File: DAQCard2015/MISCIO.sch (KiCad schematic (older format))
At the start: 25 parts, among them K1 1462042-8, P3 miniDIL20, P4 LEMO_EPY.00.250.NTN, P5 LEMO_EPY.00.250.NTN, P6 FAN, P9 SMA, Q1 Q_NPN_BCE, Q2 NPN, U24 MCP65R41

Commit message: Various updates to DAQ board focusing on power system
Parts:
- removed D3: LED, symbol LED
- removed JP1: JUMPER, symbol JUMPER
- removed P9: SMA, symbol BNC
- added D1: Dialight_5690101372F, extras:Dialight_5690101372F, symbol Dialight_5690101372F
- added P9: SHV, extras:TE_1217133-1, symbol SHV
- added R50, R51, R52: R, Resistors_SMD:R_0603, symbol R
- C70: footprint (none) -> Capacitors_SMD:C_1812
- D2: footprint (none) -> Diodes_SMD:SMA_Standard
- K1: footprint (none) -> extras:1462042-8
- Q2: footprint (none) -> Housings_SOT-23_SOT-143_TSOT-6:SOT-23
- R55: footprint Resistors_SMD:R_0805 -> Resistors_SMD:R_1206
- R57, R58, R59, R60: footprint (none) -> Resistors_SMD:R_1206
- R61, R62: footprint (none) -> Resistors_SMD:R_0603
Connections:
- net labels added: LED0, LED1
- wire segments 81 -> 84
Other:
- note added: "HV Rated > 600V"
- note removed: "HV Rated > 250V"
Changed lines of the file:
@@
 $EndComp
 $Comp
-L GND #PWR1
+L GND #PWR01
 U 1 1 55F022ED
 P 8100 5400
-F 0 "#PWR1" H 8100 5150 50  0001 C CNN
+F 0 "#PWR01" H 8100 5150 50  0001 C CNN
 F 1 "GND" H 8100 5250 50  0000 C CNN
 F 2 "" H 8100 5400 60  0000 C CNN
@@
 $EndComp
 $Comp
-L GND #PWR2
+L GND #PWR02
 U 1 1 55F02317
 P 8600 5300
-F 0 "#PWR2" H 8600 5050 50  0001 C CNN
+F 0 "#PWR02" H 8600 5050 50  0001 C CNN
 F 1 "GND" H 8600 5150 50  0000 C CNN
 F 2 "" H 8600 5300 60  0000 C CNN
@@
 F 0 "R55" V 9130 4950 50  0000 C CNN
 F 1 "50k" V 9050 4950 50  0000 C CNN
-F 2 "Resistors_SMD:R_0805" V 8980 4950 30  0001 C CNN
+F 2 "Resistors_SMD:R_1206" V 8980 4950 30  0001 C CNN
 F 3 "" H 9050 4950 30  0000 C CNN
 	1    9050 4950
@@
 F 0 "K1" H 3400 2500 60  0000 C CNN
 F 1 "1462042-8" H 3200 1900 60  0000 C CNN
-F 2 "" H 3200 2200 60  0001 C CNN
+F 2 "extras:1462042-8" H 3200 2200 60  0001 C CNN
 F 3 "" H 3200 2200 60  0000 C CNN
 	1    3200 2200
@@
 F 0 "R59" V 2630 2050 50  0000 C CNN
 F 1 "470k" V 2550 2050 50  0000 C CNN
-F 2 "" V 2480 2050 30  0001 C CNN
+F 2 "Resistors_SMD:R_1206" V 2480 2050 30  0001 C CNN
 F 3 "" H 2550 2050 30  0000 C CNN
 	1    2550 2050
@@
 F 0 "R57" V 2330 2400 50  0000 C CNN
 F 1 "470k" V 2250 2400 50  0000 C CNN
-F 2 "" V 2180 2400 30  0001 C CNN
+F 2 "Resistors_SMD:R_1206" V 2180 2400 30  0001 C CNN
 F 3 "" H 2250 2400 30  0000 C CNN
 	1    2250 2400
 	0    1    1    0
 $EndComp
-$Comp
-L BNC P9
-U 1 1 55F41081
-P 1800 2150
-F 0 "P9" H 1810 2270 50  0000 C CNN
-F 1 "SMA" V 1910 2090 50  0000 C CNN
-F 2 "" H 1800 2150 60  0001 C CNN
-F 3 "" H 1800 2150 60  0000 C CNN
-	1    1800 2150
-	-1   0    0    -1
-$EndComp
-Text GLabel 2750 2600 1    60   Input ~ 0
+Text GLabel 1350 2400 0    60   Input ~ 0
 GND
 $Comp
@@
 F 0 "C70" H 1625 2700 50  0000 L CNN
 F 1 "22nF" H 1625 2500 50  0000 L CNN
-F 2 "" H 1638 2450 30  0001 C CNN
+F 2 "Capacitors_SMD:C_1812" H 1638 2450 30  0001 C CNN
 F 3 "" H 1600 2600 60  0000 C CNN
 	1    1600 2600
@@
 F 0 "R60" V 2780 2800 50  0000 C CNN
 F 1 "51k" V 2700 2800 50  0000 C CNN
-F 2 "" V 2630 2800 30  0001 C CNN
+F 2 "Resistors_SMD:R_1206" V 2630 2800 30  0001 C CNN
 F 3 "" H 2700 2800 30  0000 C CNN
 	1    2700 2800
@@
 F 0 "R58" V 2380 2800 50  0000 C CNN
 F 1 "51k" V 2300 2800 50  0000 C CNN
-F 2 "" V 2230 2800 30  0001 C CNN
+F 2 "Resistors_SMD:R_1206" V 2230 2800 30  0001 C CNN
 F 3 "" H 2300 2800 30  0000 C CNN
 	1    2300 2800
@@
 F 0 "D2" H 3900 2580 50  0000 L CNN
 F 1 "D" H 3950 2400 50  0000 L CNN
-F 2 "" V 3950 2500 60  0001 C CNN
+F 2 "Diodes_SMD:SMA_Standard" V 3950 2500 60  0001 C CNN
 F 3 "" V 3950 2500 60  0000 C CNN
 	1    3950 2500
@@
 F 0 "Q2" H 4350 3000 50  0000 R CNN
 F 1 "NPN" H 4400 2900 50  0000 R CNN
-F 2 "" H 4250 3050 29  0001 C CNN
+F 2 "Housings_SOT-23_SOT-143_TSOT-6:SOT-23" H 4250 3050 29  0001 C CNN
 F 3 "" H 4050 2950 60  0000 C CNN
 	1    4050 2950
@@
 Text GLabel 3950 3250 3    60   Input ~ 0
 GND
-$Comp
-L LED D3
-U 1 1 55F438E7
-P 5150 3200
-F 0 "D3" H 5150 3300 50  0000 C CNN
-F 1 "LED" H 5150 3100 50  0000 C CNN
-F 2 "" H 5150 3200 60  0001 C CNN
-F 3 "" H 5150 3200 60  0000 C CNN
-	1    5150 3200
-	0    -1   -1   0
-$EndComp
-$Comp
-L R R62
-U 1 1 55F43A0B
-P 4850 2950
-F 0 "R62" V 4930 2950 50  0000 C CNN
-F 1 "R" V 4850 2950 50  0000 C CNN
-F 2 "" V 4780 2950 30  0001 C CNN
-F 3 "" H 4850 2950 30  0000 C CNN
-	1    4850 2950
-	0    1    1    0
-$EndComp
-Text GLabel 5150 3450 3    60   Input ~ 0
-GND
-Text Label 4600 2650 0    60   ~ 0
-HV_control
 Text GLabel 3950 2100 1    60   Input ~ 0
 5Vdig
@@
 	2400 2050 2400 2400
 Wire Wire Line
-	1600 2400 2100 2400
+	1350 2400 2100 2400
 Wire Wire Line
 	3500 2100 3700 2100
@@
 	1600 2800 1600 2750
 Connection ~ 1600 2800
-Connection ~ 1800 2400
-Wire Wire Line
-	1800 2350 1800 2600
 Wire Wire Line
 	1950 2150 2900 2150
-Wire Wire Line
-	1800 2600 2150 2600
 Wire Wire Line
 	2900 2350 2900 2650
@@
 Wire Wire Line
 	3950 3150 3950 3250
-Wire Wire Line
-	5150 2950 5150 3000
-Wire Wire Line
-	5150 2950 5000 2950
-Wire Wire Line
-	4700 2950 4600 2950
-Wire Wire Line
-	5150 3400 5150 3450
-Wire Wire Line
-	4600 2950 4600 2650
-Connection ~ 4600 2950
-$Comp
-L JUMPER JP1
-U 1 1 55F41215
-P 2450 2600
-F 0 "JP1" H 2450 2750 50  0000 C CNN
-F 1 "JUMPER" H 2450 2520 50  0000 C CNN
-F 2 "" H 2450 2600 60  0001 C CNN
-F 3 "" H 2450 2600 60  0000 C CNN
-	1    2450 2600
-	1    0    0    -1
-$EndComp
 Text Notes 650  2650 0    60   ~ 0
-HV Rated > 250V
+HV Rated > 600V
 $Comp
 L R R61
@@
 F 0 "R61" V 4530 2950 50  0000 C CNN
 F 1 "5k1" V 4450 2950 50  0000 C CNN
-F 2 "" V 4380 2950 30  0001 C CNN
+F 2 "Resistors_SMD:R_0603" V 4380 2950 30  0001 C CNN
 F 3 "" H 4450 2950 30  0000 C CNN
 	1    4450 2950
@@
 Wire Wire Line
 	4300 2950 4250 2950
+$Comp
+L SHV P9
+U 1 1 55F913FA
+P 1800 2150
+F 0 "P9" H 1810 2270 50  0000 C CNN
+F 1 "SHV" H 1900 2050 50  0000 C CNN
+F 2 "extras:TE_1217133-1" H 1800 2150 60  0001 C CNN
+F 3 "" H 1800 2150 60  0000 C CNN
+	1    1800 2150
+	-1   0    0    1
+$EndComp
+Connection ~ 1600 2400
+$Comp
+L Dialight_5690101372F D1
+U 1 1 55FA5BD1
+P 1750 5050
+F 0 "D1" V 1650 5050 60  0000 C CNN
+F 1 "Dialight_5690101372F" V 1900 5050 60  0001 C CNN
+F 2 "extras:Dialight_5690101372F" H 1750 5050 60  0001 C CNN
+F 3 "" H 1750 5050 60  0000 C CNN
+	1    1750 5050
+	1    0    0    -1
+$EndComp
+$Comp
+L Dialight_5690101372F D1
+U 3 1 55FA5D9B
+P 2350 5050
+F 0 "D1" V 2250 5050 60  0000 C CNN
+F 1 "Dialight_5690101372F" V 2500 5050 60  0001 C CNN
+F 2 "extras:Dialight_5690101372F" H 2350 5050 60  0001 C CNN
+F 3 "" H 2350 5050 60  0000 C CNN
+	3    2350 5050
+	1    0    0    -1
+$EndComp
+$Comp
+L Dialight_5690101372F D1
+U 4 1 55FA5E02
+P 2650 5050
+F 0 "D1" V 2550 5050 60  0000 C CNN
+F 1 "Dialight_5690101372F" V 2800 5050 60  0001 C CNN
+F 2 "extras:Dialight_5690101372F" H 2650 5050 60  0001 C CNN
+F 3 "" H 2650 5050 60  0000 C CNN
+	4    2650 5050
+	1    0    0    -1
+$EndComp
+Text GLabel 1750 4400 1    60   Input ~ 0
+5Vdig
+Wire Wire Line
+	2650 5350 2650 5150
+Wire Wire Line
+	1450 5350 2650 5350
+Text GLabel 1450 5350 0    60   Input ~ 0
+GND
+Wire Wire Line
+	2350 5150 2350 5350
+Connection ~ 2350 5350
+Wire Wire Line
+	2050 5150 2050 5350
+Connection ~ 2050 5350
+Wire Wire Line
+	1750 5150 1750 5350
+Connection ~ 1750 5350
+Text GLabel 4750 2950 2    60   Input ~ 0
+HV_control
+Wire Wire Line
+	4750 2950 4600 2950
+Text GLabel 2050 4400 1    60   Input ~ 0
+HV_control
+$Comp
+L R R50
+U 1 1 55FA73A0
+P 1750 4550
+F 0 "R50" V 1830 4550 50  0000 C CNN
+F 1 "R" V 1750 4550 50  0000 C CNN
+F 2 "Resistors_SMD:R_0603" V 1680 4550 30  0001 C CNN
+F 3 "" H 1750 4550 30  0000 C CNN
+	1    1750 4550
+	1    0    0    -1
+$EndComp
+$Comp
+L R R51
+U 1 1 55FA7424
+P 2050 4550
+F 0 "R51" V 2130 4550 50  0000 C CNN
+F 1 "R" V 2050 4550 50  0000 C CNN
+F 2 "Resistors_SMD:R_0603" V 1980 4550 30  0001 C CNN
+F 3 "" H 2050 4550 30  0000 C CNN
+	1    2050 4550
+	1    0    0    -1
+$EndComp
+$Comp
+L R R52
+U 1 1 55FA749A
+P 2350 4550
+F 0 "R52" V 2430 4550 50  0000 C CNN
+F 1 "R" V 2350 4550 50  0000 C CNN
+F 2 "Resistors_SMD:R_0603" V 2280 4550 30  0001 C CNN
+F 3 "" H 2350 4550 30  0000 C CNN
+	1    2350 4550
+	1    0    0    -1
+$EndComp
+$Comp
+L R R62
+U 1 1 55FA7511
+P 2650 4550
+F 0 "R62" V 2730 4550 50  0000 C CNN
+F 1 "R" V 2650 4550 50  0000 C CNN
+F 2 "Resistors_SMD:R_0603" V 2580 4550 30  0001 C CNN
+F 3 "" H 2650 4550 30  0000 C CNN
+	1    2650 4550
+	1    0    0    -1
+$EndComp
+$Comp
+L Dialight_5690101372F D1
+U 2 1 55FA5C66
+P 2050 5050
+F 0 "D1" V 1950 5050 60  0000 C CNN
+F 1 "Dialight_5690101372F" V 2200 5050 60  0001 C CNN
+F 2 "extras:Dialight_5690101372F" H 2050 5050 60  0001 C CNN
+F 3 "" H 2050 5050 60  0000 C CNN
+	2    2050 5050
+	1    0    0    -1
+$EndComp
+Wire Wire Line
+	1750 4700 1750 4850
+Wire Wire Line
+	2050 4700 2050 4850
+Wire Wire Line
+	2350 4700 2350 4850
+Wire Wire Line
+	2650 4700 2650 4850
+Text GLabel 2350 4400 1    60   Input ~ 0
+LED0
+Text GLabel 2650 4400 1    60   Input ~ 0
+LED1
 $EndSCHEMATC

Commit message: Updates to DAQ board focusing on Support electronics
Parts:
- removed Q1: Q_NPN_BCE, Housings_SOT-23_SOT-143_TSOT-6:SOT-23, symbol Q_NPN_BCE
- added Q1: Q_NPN_BCE_REV, symbol Q_NPN_BCE_REV
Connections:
- wire segments 84 -> 82
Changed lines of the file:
@@
 $Descr A4 11693 8268
 encoding utf-8
-Sheet 12 13
+Sheet 3 13
 Title ""
 Date ""
@@
 $EndComp
 $Comp
-L Q_NPN_BCE Q1
-U 1 1 55F036FA
-P 10200 4650
-F 0 "Q1" H 10500 4700 50  0000 R CNN
-F 1 "Q_NPN_BCE" H 10800 4600 50  0000 R CNN
-F 2 "Housings_SOT-23_SOT-143_TSOT-6:SOT-23" H 10400 4750 29  0001 C CNN
-F 3 "" H 10200 4650 60  0000 C CNN
-	1    10200 4650
-	1    0    0    -1
-$EndComp
-$Comp
 L R R56
 U 1 1 55F03778
@@
 Text GLabel 3950 2100 1    60   Input ~ 0
 5Vdig
-Text Label 1350 2800 0    60   ~ 0
-Vbias
 Wire Wire Line
 	8450 2450 8450 3400
@@
 	8450 2850 8500 2850
 Wire Wire Line
-	10050 1900 9750 1900
-Wire Wire Line
-	9750 1900 9750 2050
-Wire Wire Line
-	9750 2050 9200 2050
-Wire Wire Line
-	9200 2150 9800 2150
-Wire Wire Line
-	9800 2150 9800 2050
-Wire Wire Line
-	9800 2050 10050 2050
+	9200 2050 10050 2050
+Wire Wire Line
+	9800 2150 9200 2150
+Wire Wire Line
+	9800 1900 9800 2150
 Wire Wire Line
 	9200 2250 9750 2250
 Wire Wire Line
-	9750 2250 9750 2500
-Wire Wire Line
-	9750 2500 9800 2500
-Wire Wire Line
-	9800 2650 9700 2650
-Wire Wire Line
-	9700 2650 9700 2350
+	9750 2250 9750 2650
 Wire Wire Line
 	9700 2350 9200 2350
@@
 Text GLabel 2650 4400 1    60   Input ~ 0
 LED1
+$Comp
+L Q_NPN_BCE_REV Q1
+U 1 1 56022DB8
+P 10200 4650
+F 0 "Q1" H 10500 4700 50  0000 R CNN
+F 1 "Q_NPN_BCE_REV" H 11000 4600 50  0000 R CNN
+F 2 "" H 10400 4750 29  0000 C CNN
+F 3 "" H 10200 4650 60  0000 C CNN
+	1    10200 4650
+	1    0    0    -1
+$EndComp
+Text GLabel 1350 2800 0    60   Input ~ 0
+Vbias
+Wire Wire Line
+	9800 1900 10050 1900
+Wire Wire Line
+	9750 2650 9800 2650
+Wire Wire Line
+	9700 2350 9700 2500
+Wire Wire Line
+	9700 2500 9800 2500
 $EndSCHEMATC

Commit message: Adds APC128 connections and voltage supplies
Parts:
- removed Q2: NPN, Housings_SOT-23_SOT-143_TSOT-6:SOT-23, symbol Q_NPN_BCE
- added Q2: SBC817-40LT1G, Housings_SOT-23_SOT-143_TSOT-6:SOT-23, symbol Q_NPN_BCE_REV
- added U19, U23: AD8534, Housings_SSOP:TSSOP-14_4.4x5mm_Pitch0.65mm, symbol AD8534
- added U22: AD5628, extras:TSSOP-16_4.4x5mm_Pitch0.65mm, symbol AD5628
- D2: value D -> SMAJ75A
- Q1: value Q_NPN_BCE_REV -> MMBT2222A-TP; footprint (none) -> Housings_SOT-23_SOT-143_TSOT-6:SOT-23
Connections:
- net labels added: Aref_A, Aref_B, DAC_A, DAC_B, DAC_C, DAC_D, DAC_E, DAC_F, DAC_G, DAC_H, RG_A, RG_B, SPI_SCL, SPI_SDA, SUPDAC_CSB, Vana_A, Vana_B, Vocm, Vthresh
- wire segments 82 -> 123
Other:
- moved on the sheet: C70, D1A, D1B, D1C, D1D, D2, K1, P3, P4, P5, P6, P9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

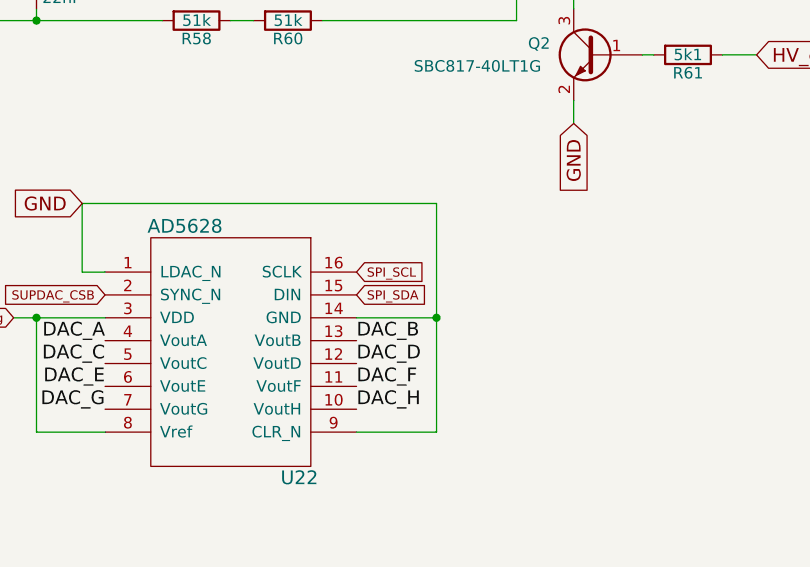
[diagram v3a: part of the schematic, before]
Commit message: Adds misc traces(gnds, SPI, etc) to DAQ board
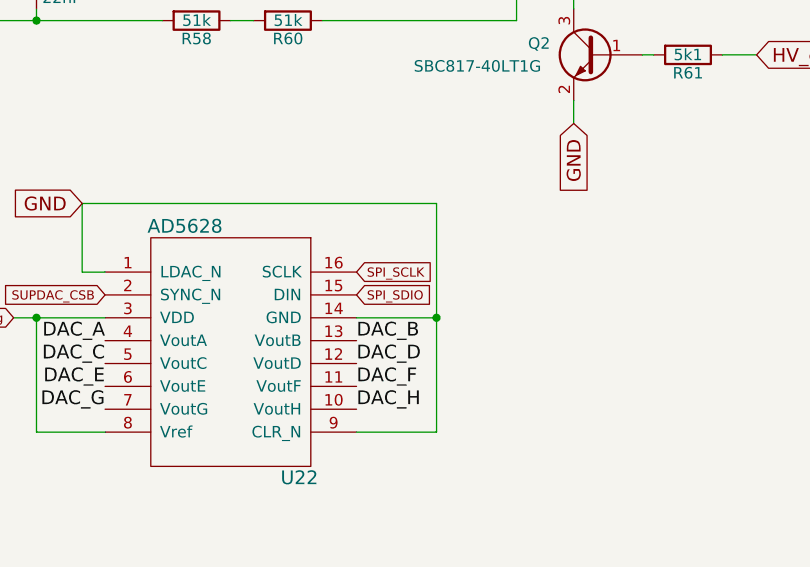
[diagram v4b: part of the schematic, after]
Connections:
- net SPI_SCL renamed SPI_SCLK
- net SPI_SDA renamed SPI_SDIO
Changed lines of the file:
@@
 Connection ~ 1650 2950
 Text GLabel 3050 2750 2    40   Input ~ 0
-SPI_SCL
+SPI_SCLK
 Text GLabel 3050 2850 2    40   Input ~ 0
-SPI_SDA
+SPI_SDIO
 Text Label 1950 3050 2    60   ~ 0
 DAC_A

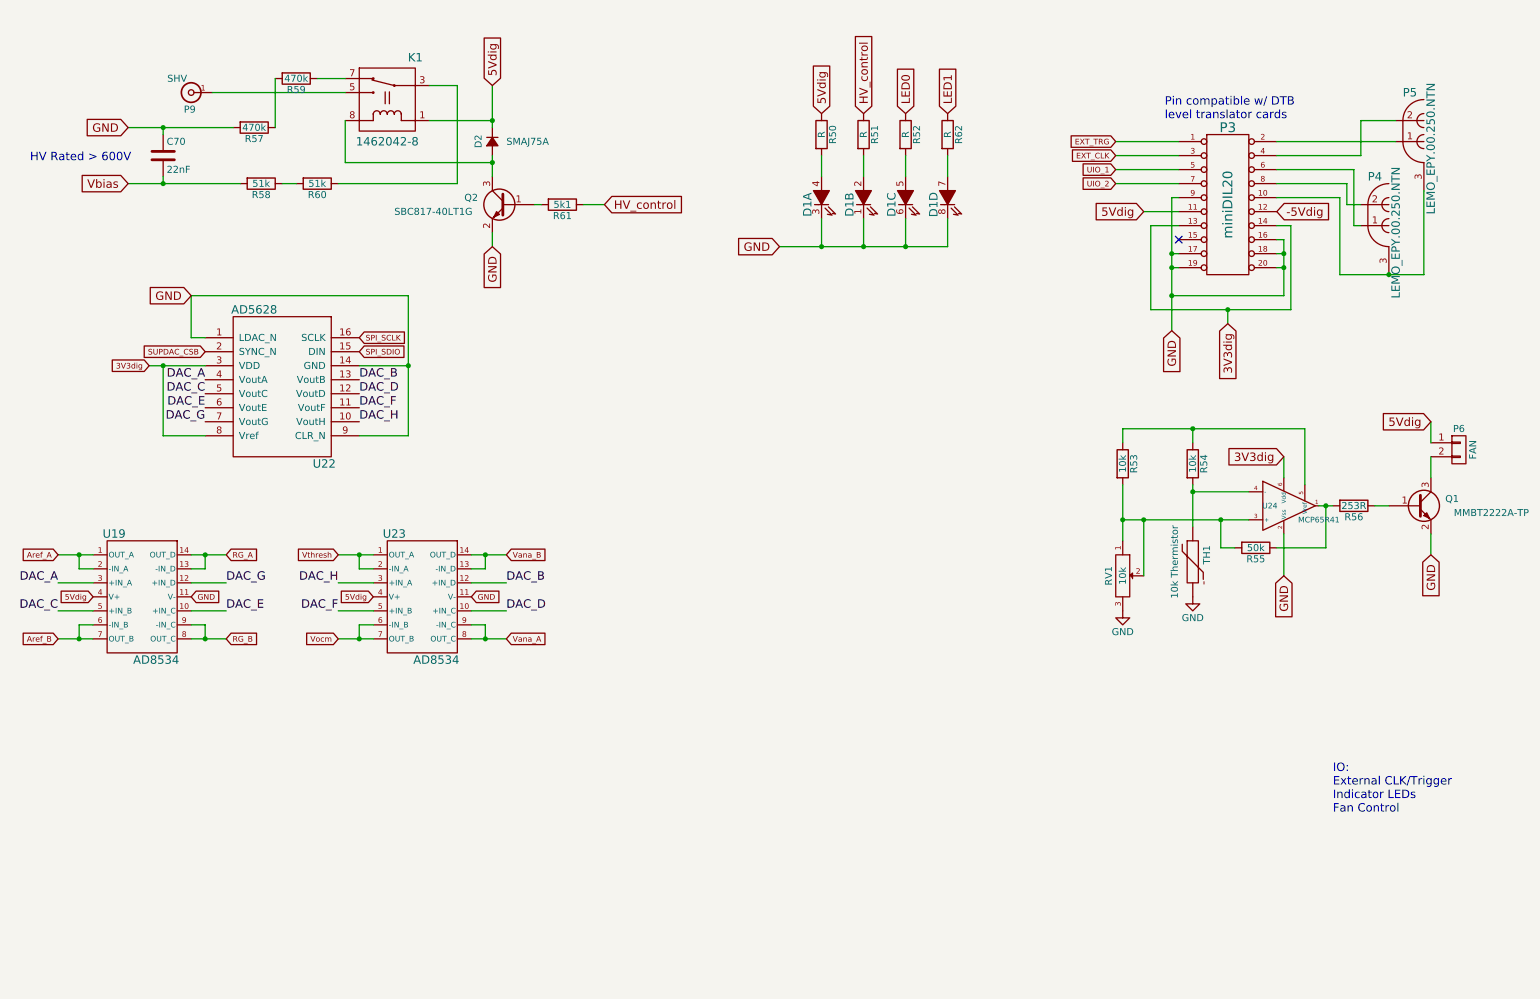
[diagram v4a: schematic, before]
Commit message: Update to DAQ Board including adding an JTAG header and hooking up external clock and trigger
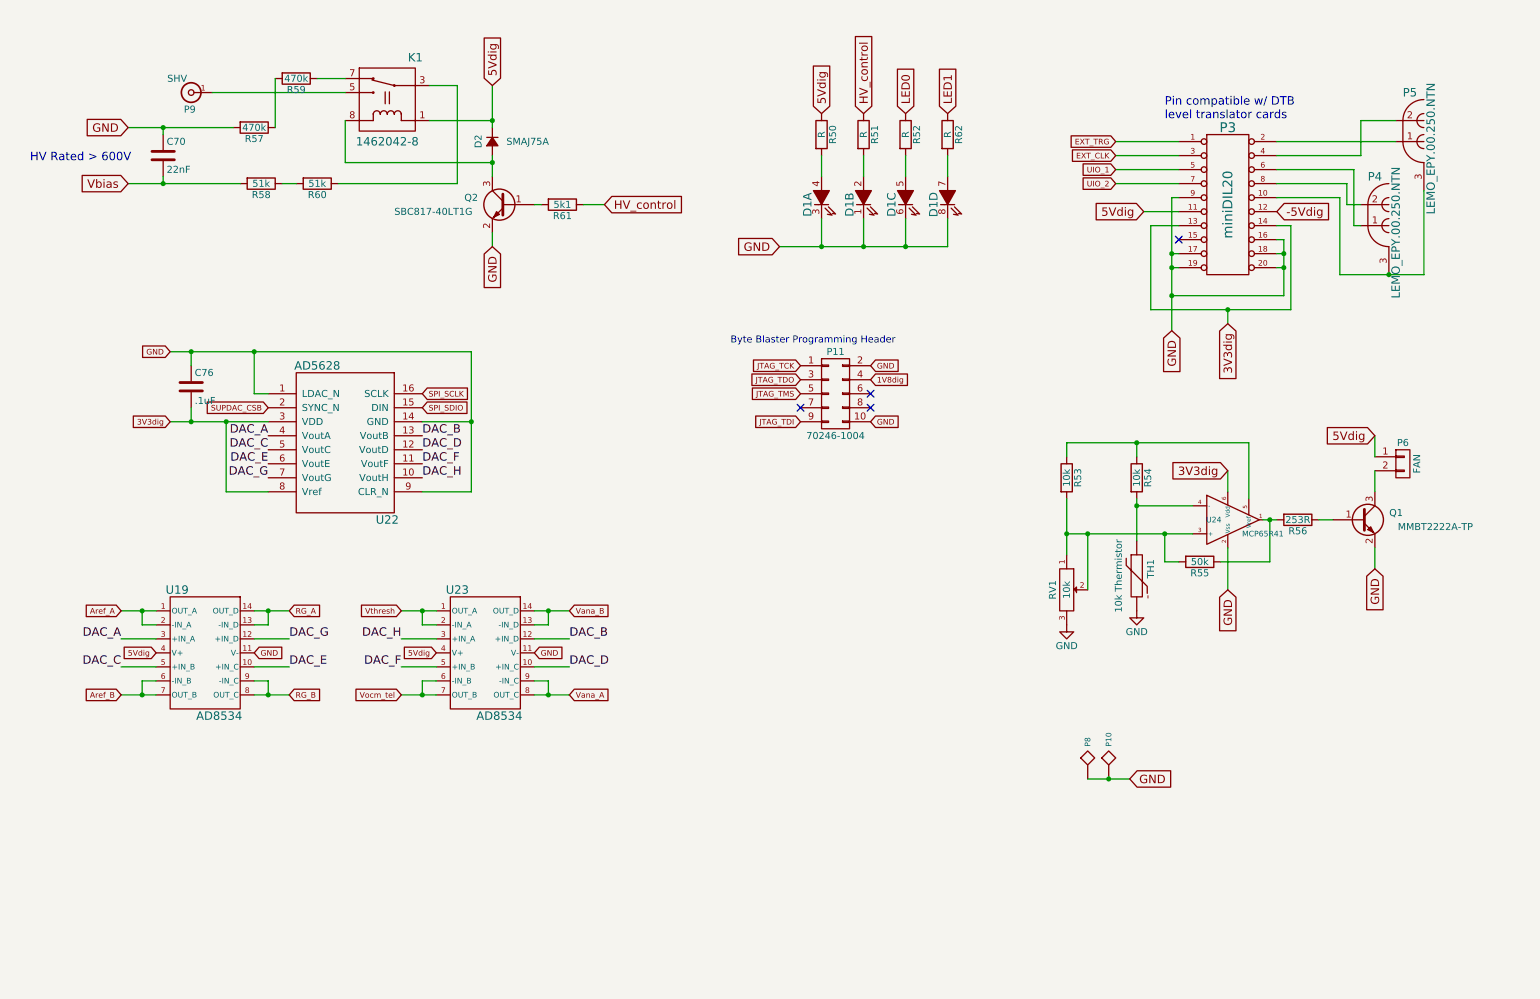
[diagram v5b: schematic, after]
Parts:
- added C76: .1uF, Capacitors_SMD:C_0603, symbol C
- added P10, P8: SPYPAD, extras:Harwin_D3082-05, symbol SPYPAD
- added P11: 70246-1004, Pin_Headers:Pin_Header_Straight_2x05, symbol CONN_02X05
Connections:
- net 3V3dig: now also C76.2
- net GND: now also C76.1, P10.1, P11.10 (P10), P11.2 (P2), P8.1
- net Vocm renamed Vocm_tel
- new net 1V8dig: P11.4 (P4)
- new net JTAG_TCK: P11.1 (P1)
- new net JTAG_TDI: P11.9 (P9)
- new net JTAG_TDO: P11.3 (P3)
- new net JTAG_TMS: P11.5 (P5)
- no-connect marks 1 -> 4
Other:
- note added: "Byte Blaster Programming Header"
- note removed: "IO:\nExternal CLK/Trigger\nIndicator LEDs\nFan Control"
- moved on the sheet: P6, Q1, R53, R54, R55, R56, RV1, TH1, U19, U22, U23, U24
